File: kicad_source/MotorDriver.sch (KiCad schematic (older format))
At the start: 53 parts, among them P1 WR-TBL_691313710002, P2 WR-TBL_691322310002, P3 WR-TBL_691313710002, P4 WR-TBL_691313710002, Q1 2N7002, Q2 IPD90P03P4L- 04, U1 IFX007T, U2 74xx08, U3 IFX007T, U4 IFX007T, U5 IFX007T

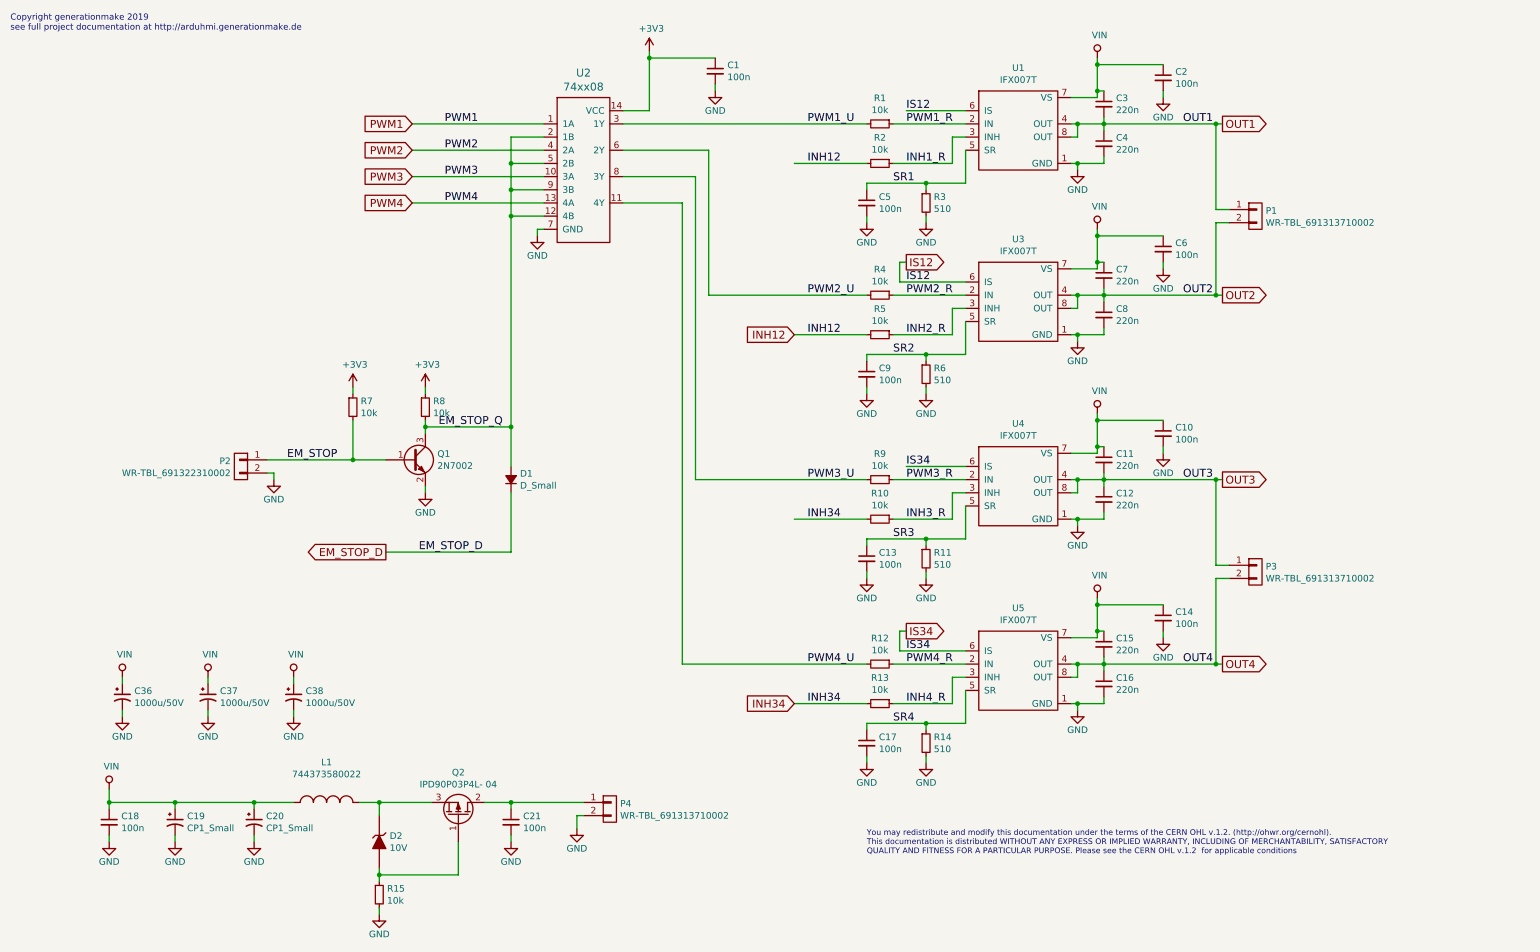
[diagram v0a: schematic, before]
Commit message: added values in schematic, generated pdf schematic
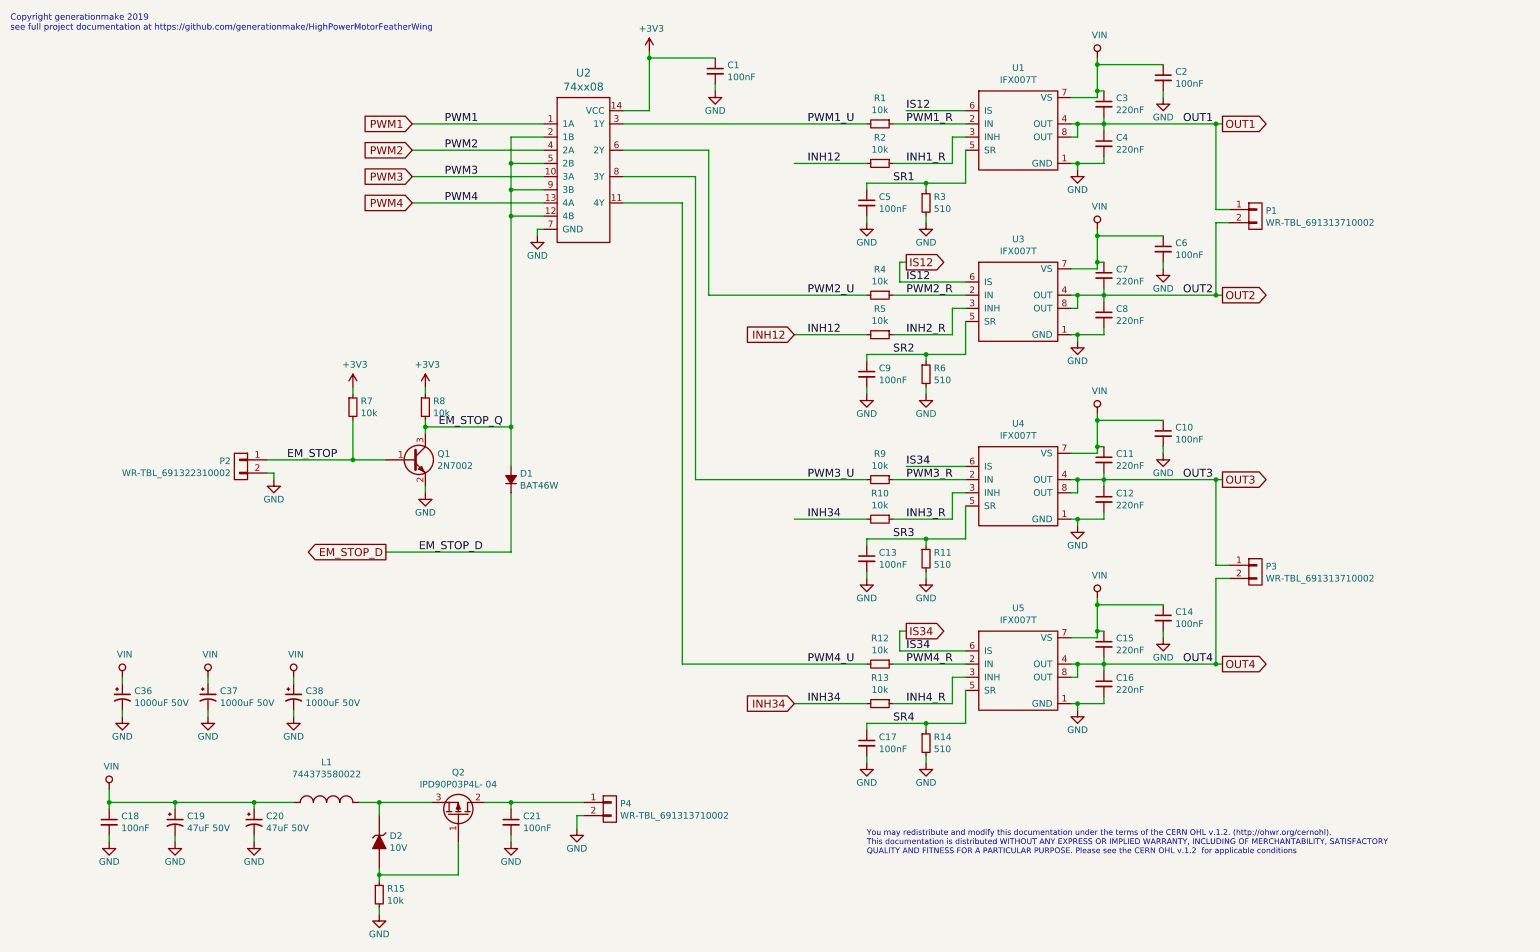
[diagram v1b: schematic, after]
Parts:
- C1, C10, C13, C14, C17, C18, C2, C21, C5, C6, C9: value 100n -> 100nF
- C11, C12, C15, C16, C3, C4, C7, C8: value 220n -> 220nF
- C19, C20: value CP1_Small -> 47uF 50V
- C36, C37, C38: value 1000u/50V -> 1000uF 50V
- D1: value D_Small -> BAT46W
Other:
- note added: "Copyright generationmake 2019\nsee full project documentation at https://github.com/generationmake/HighPowerMotorFeatherWing"
- note removed: "Copyright generationmake 2019\nsee full project documentation at http://arduhmi.generationmake.de"
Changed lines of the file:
@@
 EESchema Schematic File Version 4
-LIBS:HighPowerMotorFeatherWing-cache
-EELAYER 26 0
+EELAYER 30 0
 EELAYER END
 $Descr A4 11693 8268
@@
 Sheet 2 5
 Title "HighPowerMotorFeatherWing"
-Date "2019-12-01"
+Date "2019-12-29"
 Rev "1.0"
 Comp "generationmake"
@@
 $EndDescr
 Text Notes 500  650  0    47   ~ 0
-Copyright generationmake 2019\nsee full project documentation at http://arduhmi.generationmake.de
+Copyright generationmake 2019\nsee full project documentation at https://github.com/generationmake/HighPowerMotorFeatherWing
 Text Notes 7000 6900 0    43   ~ 0
 You may redistribute and modify this documentation under the terms of the CERN OHL v.1.2. (http://ohwr.org/cernohl). \nThis documentation is distributed WITHOUT ANY EXPRESS OR IMPLIED WARRANTY, INCLUDING OF MERCHANTABILITY, SATISFACTORY \nQUALITY AND FITNESS FOR A PARTICULAR PURPOSE. Please see the CERN OHL v.1.2  for applicable conditions
@@
 P 7000 1950
 F 0 "C5" H 7092 1996 50  0000 L CNN
-F 1 "100n" H 7092 1905 50  0000 L CNN
+F 1 "100nF" H 7092 1905 50  0000 L CNN
 F 2 "capacitors:C_0603" H 7000 1800 50  0001 C CNN
 F 3 "" H 7000 1950 50  0000 C CNN
@@
 P 7000 3250
 F 0 "C9" H 7092 3296 50  0000 L CNN
-F 1 "100n" H 7092 3205 50  0000 L CNN
+F 1 "100nF" H 7092 3205 50  0000 L CNN
 F 2 "capacitors:C_0603" H 7000 3100 50  0001 C CNN
 F 3 "" H 7000 3250 50  0000 C CNN
@@
 P 7000 4650
 F 0 "C13" H 7092 4696 50  0000 L CNN
-F 1 "100n" H 7092 4605 50  0000 L CNN
+F 1 "100nF" H 7092 4605 50  0000 L CNN
 F 2 "capacitors:C_0603" H 7000 4500 50  0001 C CNN
 F 3 "" H 7000 4650 50  0000 C CNN
@@
 P 4300 6650
 F 0 "C21" H 4392 6696 50  0000 L CNN
-F 1 "100n" H 4392 6605 50  0000 L CNN
+F 1 "100nF" H 4392 6605 50  0000 L CNN
 F 2 "capacitors:C_0603" H 4300 6500 50  0001 C CNN
 F 3 "" H 4300 6650 50  0000 C CNN
@@
 P 8800 5300
 F 0 "C15" H 8892 5346 50  0000 L CNN
-F 1 "220n" H 8892 5255 50  0000 L CNN
+F 1 "220nF" H 8892 5255 50  0000 L CNN
 F 2 "capacitors:C_0603" H 8800 5150 50  0001 C CNN
 F 3 "" H 8800 5300 50  0000 C CNN
@@
 P 8800 5600
 F 0 "C16" H 8892 5646 50  0000 L CNN
-F 1 "220n" H 8892 5555 50  0000 L CNN
+F 1 "220nF" H 8892 5555 50  0000 L CNN
 F 2 "capacitors:C_0603" H 8800 5450 50  0001 C CNN
 F 3 "" H 8800 5600 50  0000 C CNN
@@
 P 8800 3900
 F 0 "C11" H 8892 3946 50  0000 L CNN
-F 1 "220n" H 8892 3855 50  0000 L CNN
+F 1 "220nF" H 8892 3855 50  0000 L CNN
 F 2 "capacitors:C_0603" H 8800 3750 50  0001 C CNN
 F 3 "" H 8800 3900 50  0000 C CNN
@@
 P 8800 4200
 F 0 "C12" H 8892 4246 50  0000 L CNN
-F 1 "220n" H 8892 4155 50  0000 L CNN
+F 1 "220nF" H 8892 4155 50  0000 L CNN
 F 2 "capacitors:C_0603" H 8800 4050 50  0001 C CNN
 F 3 "" H 8800 4200 50  0000 C CNN
@@
 P 8800 2500
 F 0 "C7" H 8892 2546 50  0000 L CNN
-F 1 "220n" H 8892 2455 50  0000 L CNN
+F 1 "220nF" H 8892 2455 50  0000 L CNN
 F 2 "capacitors:C_0603" H 8800 2350 50  0001 C CNN
 F 3 "" H 8800 2500 50  0000 C CNN
@@
 P 8800 2800
 F 0 "C8" H 8892 2846 50  0000 L CNN
-F 1 "220n" H 8892 2755 50  0000 L CNN
+F 1 "220nF" H 8892 2755 50  0000 L CNN
 F 2 "capacitors:C_0603" H 8800 2650 50  0001 C CNN
 F 3 "" H 8800 2800 50  0000 C CNN
@@
 P 8800 1200
 F 0 "C3" H 8892 1246 50  0000 L CNN
-F 1 "220n" H 8892 1155 50  0000 L CNN
+F 1 "220nF" H 8892 1155 50  0000 L CNN
 F 2 "capacitors:C_0603" H 8800 1050 50  0001 C CNN
 F 3 "" H 8800 1200 50  0000 C CNN
@@
 P 8800 1500
 F 0 "C4" H 8892 1546 50  0000 L CNN
-F 1 "220n" H 8892 1455 50  0000 L CNN
+F 1 "220nF" H 8892 1455 50  0000 L CNN
 F 2 "capacitors:C_0603" H 8800 1350 50  0001 C CNN
 F 3 "" H 8800 1500 50  0000 C CNN
@@
 P 9250 1000
 F 0 "C2" H 9342 1046 50  0000 L CNN
-F 1 "100n" H 9342 955 50  0000 L CNN
+F 1 "100nF" H 9342 955 50  0000 L CNN
 F 2 "capacitors:C_0603" H 9250 850 50  0001 C CNN
 F 3 "" H 9250 1000 50  0000 C CNN
@@
 P 9250 2300
 F 0 "C6" H 9342 2346 50  0000 L CNN
-F 1 "100n" H 9342 2255 50  0000 L CNN
+F 1 "100nF" H 9342 2255 50  0000 L CNN
 F 2 "capacitors:C_0603" H 9250 2150 50  0001 C CNN
 F 3 "" H 9250 2300 50  0000 C CNN
@@
 P 9250 3700
 F 0 "C10" H 9342 3746 50  0000 L CNN
-F 1 "100n" H 9342 3655 50  0000 L CNN
+F 1 "100nF" H 9342 3655 50  0000 L CNN
 F 2 "capacitors:C_0603" H 9250 3550 50  0001 C CNN
 F 3 "" H 9250 3700 50  0000 C CNN
@@
 P 9250 5100
 F 0 "C14" H 9342 5146 50  0000 L CNN
-F 1 "100n" H 9342 5055 50  0000 L CNN
+F 1 "100nF" H 9342 5055 50  0000 L CNN
 F 2 "capacitors:C_0603" H 9250 4950 50  0001 C CNN
 F 3 "" H 9250 5100 50  0000 C CNN
@@
 P 5850 950
 F 0 "C1" H 5942 996 50  0000 L CNN
-F 1 "100n" H 5942 905 50  0000 L CNN
+F 1 "100nF" H 5942 905 50  0000 L CNN
 F 2 "capacitors:C_0603" H 5850 800 50  0001 C CNN
 F 3 "" H 5850 950 50  0000 C CNN
@@
 P 4300 4050
 F 0 "D1" V 4346 3982 50  0000 R CNN
-F 1 "D_Small" V 4255 3982 50  0000 R CNN
+F 1 "BAT46W" V 4255 3982 50  0000 R CNN
 F 2 "diodes:SOD-123" V 4300 4050 50  0001 C CNN
 F 3 "" V 4300 4050 50  0000 C CNN
@@
 P 7000 6050
 F 0 "C17" H 7092 6096 50  0000 L CNN
-F 1 "100n" H 7092 6005 50  0000 L CNN
+F 1 "100nF" H 7092 6005 50  0000 L CNN
 F 2 "capacitors:C_0603" H 7000 5900 50  0001 C CNN
 F 3 "" H 7000 6050 50  0000 C CNN
@@
 P 2350 6650
 F 0 "C20" H 2441 6696 50  0000 L CNN
-F 1 "CP1_Small" H 2441 6605 50  0000 L CNN
+F 1 "47uF 50V" H 2441 6605 50  0000 L CNN
 F 2 "capacitors:TantalC_SizeD_EIA-7343_Wave" H 2450 6450 50  0001 C CNN
 F 3 "" H 2350 6650 50  0000 C CNN
@@
 P 1750 6650
 F 0 "C19" H 1841 6696 50  0000 L CNN
-F 1 "CP1_Small" H 1841 6605 50  0000 L CNN
+F 1 "47uF 50V" H 1841 6605 50  0000 L CNN
 F 2 "capacitors:TantalC_SizeD_EIA-7343_Wave" H 1850 6450 50  0001 C CNN
 F 3 "" H 1750 6650 50  0000 C CNN
@@
 P 1250 6650
 F 0 "C18" H 1342 6696 50  0000 L CNN
-F 1 "100n" H 1342 6605 50  0000 L CNN
+F 1 "100nF" H 1342 6605 50  0000 L CNN
 F 2 "capacitors:C_0603" H 1250 6500 50  0001 C CNN
 F 3 "" H 1250 6650 50  0000 C CNN
@@
 P 1350 5700
 F 0 "C36" H 1441 5746 50  0000 L CNN
-F 1 "1000u/50V" H 1441 5655 50  0000 L CNN
+F 1 "1000uF 50V" H 1441 5655 50  0000 L CNN
 F 2 "capacitors:C_elec_THT_16x25_RM7.5" H 1450 5500 50  0001 C CNN
 F 3 "" H 1350 5700 50  0000 C CNN
@@
 P 2000 5700
 F 0 "C37" H 2091 5746 50  0000 L CNN
-F 1 "1000u/50V" H 2091 5655 50  0000 L CNN
+F 1 "1000uF 50V" H 2091 5655 50  0000 L CNN
 F 2 "capacitors:C_elec_THT_16x25_RM7.5" H 2100 5500 50  0001 C CNN
 F 3 "" H 2000 5700 50  0000 C CNN
@@
 P 2650 5700
 F 0 "C38" H 2741 5746 50  0000 L CNN
-F 1 "1000u/50V" H 2741 5655 50  0000 L CNN
+F 1 "1000uF 50V" H 2741 5655 50  0000 L CNN
 F 2 "capacitors:C_elec_THT_16x25_RM7.5" H 2750 5500 50  0001 C CNN
 F 3 "" H 2650 5700 50  0000 C CNN
